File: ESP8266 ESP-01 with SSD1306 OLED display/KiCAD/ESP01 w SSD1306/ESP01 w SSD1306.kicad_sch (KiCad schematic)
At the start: 6 parts

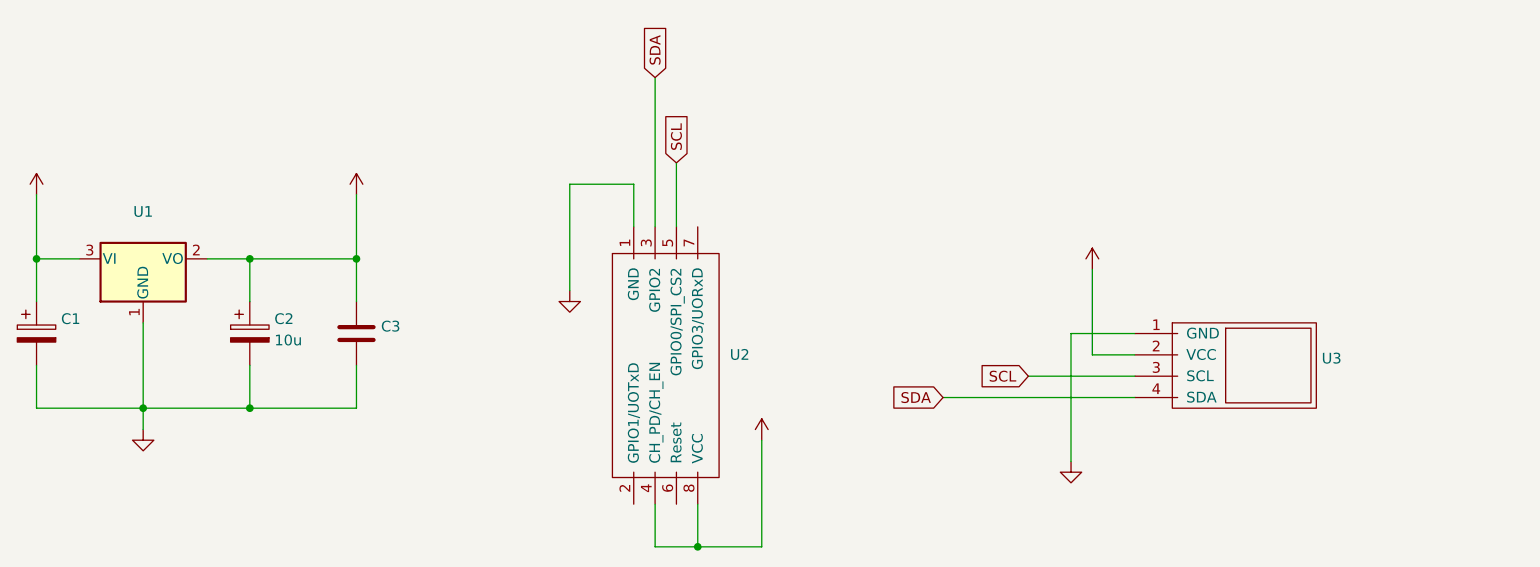
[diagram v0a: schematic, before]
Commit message: page settings n espScale
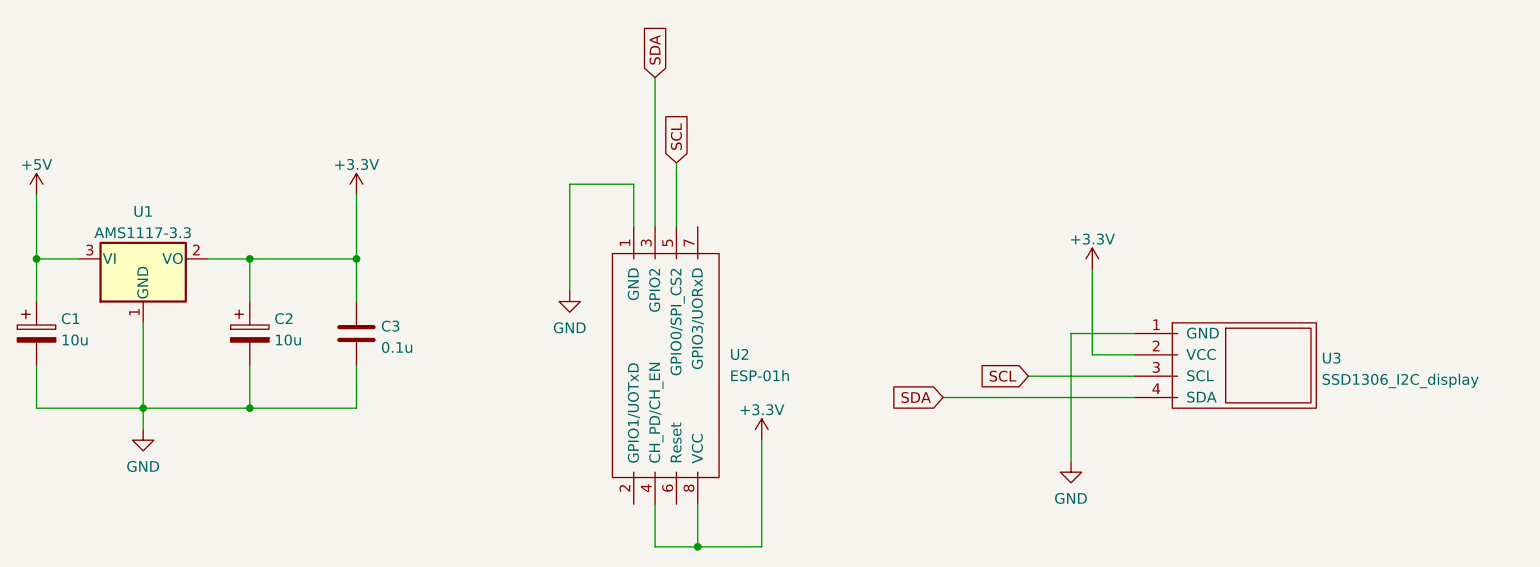
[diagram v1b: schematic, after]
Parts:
- C1: value (none) -> 10u; footprint (none) -> My_Misc:CP_Radial_D5.0mm_P2.00mm_larger
- C2: footprint (none) -> My_Misc:CP_Radial_D5.0mm_P2.00mm_larger
- C3: value (none) -> 0.1u; footprint (none) -> My_Misc:C_Disc_D3.0mm_W1.6mm_P2.50mm_larg
- U1: value (none) -> AMS1117-3.3; footprint (none) -> Package_TO_SOT_SMD:SOT-223-3_TabPin2
- U2: value (none) -> ESP-01h; footprint (none) -> My_Arduino:ESP-01_w_pin_socket_large
- U3: value (none) -> SSD1306_I2C_display; footprint (none) -> My_Parts:SSD1306_I2C_0.96_OLED_display_large
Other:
- title: (none) -> ESP01 w SSD1306
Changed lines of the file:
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@@
 (kicad_sch (version 20211123) (generator eeschema)
   (paper "A4")
+  (title_block
+    (title "ESP01 w SSD1306")
+    (date "2022-09-18")
+    (rev "0.1")
+  )
   (junction (at 68.58 93.98) (diameter 0) (color 0 0 0 0)
   )
@@
       (effects (font (size 1.27 1.27)) hide)
     )
-    (property "Value" "" (id 1) (at 81.28 65.0042 0))
+    (property "Value" "+3.3V" (id 1) (at 81.28 65.0042 0))
     (property "Footprint" "" (id 2) (at 81.28 68.58 0)
       (effects (font (size 1.27 1.27)) hide)
@@
       (effects (font (size 1.27 1.27)) (justify left))
     )
-    (property "Value" "" (id 1) (at 84.201 86.7922 0)
-      (effects (font (size 1.27 1.27)) (justify left))
-    )
-    (property "Footprint" "" (id 2) (at 82.2452 88.9 0)
+    (property "Value" "0.1u" (id 1) (at 84.201 86.7922 0)
+      (effects (font (size 1.27 1.27)) (justify left))
+    )
+    (property "Footprint" "My_Misc:C_Disc_D3.0mm_W1.6mm_P2.50mm_larg" (id 2) (at 82.2452 88.9 0)
       (effects (font (size 1.27 1.27)) hide)
     )
@@
       (effects (font (size 1.27 1.27)) hide)
     )
-    (property "Value" "" (id 1) (at 106.68 84.4534 0))
+    (property "Value" "GND" (id 1) (at 106.68 84.4534 0))
     (property "Footprint" "" (id 2) (at 106.68 80.01 0)
       (effects (font (size 1.27 1.27)) hide)
@@
       (effects (font (size 1.27 1.27)) hide)
     )
-    (property "Value" "" (id 1) (at 129.54 94.2142 0))
+    (property "Value" "+3.3V" (id 1) (at 129.54 94.2142 0))
     (property "Footprint" "" (id 2) (at 129.54 97.79 0)
       (effects (font (size 1.27 1.27)) hide)
@@
       (effects (font (size 1.27 1.27)) hide)
     )
-    (property "Value" "" (id 1) (at 43.18 65.0042 0))
+    (property "Value" "+5V" (id 1) (at 43.18 65.0042 0))
     (property "Footprint" "" (id 2) (at 43.18 68.58 0)
       (effects (font (size 1.27 1.27)) hide)
@@
       (effects (font (size 1.27 1.27)) (justify left))
     )
-    (property "Value" "" (id 1) (at 196.215 90.6022 0)
-      (effects (font (size 1.27 1.27)) (justify left))
-    )
-    (property "Footprint" "" (id 2) (at 179.705 82.55 0)
+    (property "Value" "SSD1306_I2C_display" (id 1) (at 196.215 90.6022 0)
+      (effects (font (size 1.27 1.27)) (justify left))
+    )
+    (property "Footprint" "My_Parts:SSD1306_I2C_0.96_OLED_display_large" (id 2) (at 179.705 82.55 0)
       (effects (font (size 1.27 1.27)) hide)
     )
@@
       (effects (font (size 1.27 1.27)) hide)
     )
-    (property "Value" "" (id 1) (at 166.37 104.7734 0))
+    (property "Value" "GND" (id 1) (at 166.37 104.7734 0))
     (property "Footprint" "" (id 2) (at 166.37 100.33 0)
       (effects (font (size 1.27 1.27)) hide)
@@
     (in_bom yes) (on_board yes) (fields_autoplaced)
     (property "Reference" "U1" (id 0) (at 55.88 70.5952 0))
-    (property "Value" "" (id 1) (at 55.88 73.1321 0))
-    (property "Footprint" "" (id 2) (at 55.88 71.12 0)
+    (property "Value" "AMS1117-3.3" (id 1) (at 55.88 73.1321 0))
+    (property "Footprint" "Package_TO_SOT_SMD:SOT-223-3_TabPin2" (id 2) (at 55.88 71.12 0)
       (effects (font (size 1.27 1.27)) hide)
     )
@@
       (effects (font (size 1.27 1.27)) hide)
     )
-    (property "Value" "" (id 1) (at 168.91 73.8942 0))
+    (property "Value" "+3.3V" (id 1) (at 168.91 73.8942 0))
     (property "Footprint" "" (id 2) (at 168.91 77.47 0)
       (effects (font (size 1.27 1.27)) hide)
@@
       (effects (font (size 1.27 1.27)) hide)
     )
-    (property "Value" "" (id 1) (at 55.88 100.9634 0))
+    (property "Value" "GND" (id 1) (at 55.88 100.9634 0))
     (property "Footprint" "" (id 2) (at 55.88 96.52 0)
       (effects (font (size 1.27 1.27)) hide)
@@
       (effects (font (size 1.27 1.27)) (justify left))
     )
-    (property "Value" "" (id 1) (at 46.101 85.9032 0)
-      (effects (font (size 1.27 1.27)) (justify left))
-    )
-    (property "Footprint" "" (id 2) (at 44.1452 88.9 0)
+    (property "Value" "10u" (id 1) (at 46.101 85.9032 0)
+      (effects (font (size 1.27 1.27)) (justify left))
+    )
+    (property "Footprint" "My_Misc:CP_Radial_D5.0mm_P2.00mm_larger" (id 2) (at 44.1452 88.9 0)
       (effects (font (size 1.27 1.27)) hide)
     )
@@
       (effects (font (size 1.27 1.27)) (justify left))
     )
-    (property "Footprint" "" (id 2) (at 69.5452 88.9 0)
+    (property "Footprint" "My_Misc:CP_Radial_D5.0mm_P2.00mm_larger" (id 2) (at 69.5452 88.9 0)
       (effects (font (size 1.27 1.27)) hide)
     )
@@
       (effects (font (size 1.27 1.27)) (justify left))
     )
-    (property "Value" "" (id 1) (at 125.73 90.1669 0)
-      (effects (font (size 1.27 1.27)) (justify left))
-    )
-    (property "Footprint" "" (id 2) (at 125.095 59.69 90)
-      (effects (font (size 1.27 1.27)) hide)
-    )
+    (property "Value" "ESP-01h" (id 1) (at 125.73 90.1669 0)
+      (effects (font (size 1.27 1.27)) (justify left))
+    )
+    (property "Footprint" "My_Arduino:ESP-01_w_pin_socket_large" (id 2) (at 125.095 59.69 90)
+      (effects (font (size 1.27 1.27)) hide)
+    )
